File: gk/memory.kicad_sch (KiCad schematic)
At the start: 18 parts, among them J4 Micro_SD_Card_Det2, U6 IS42S16320F-7TLI-TR

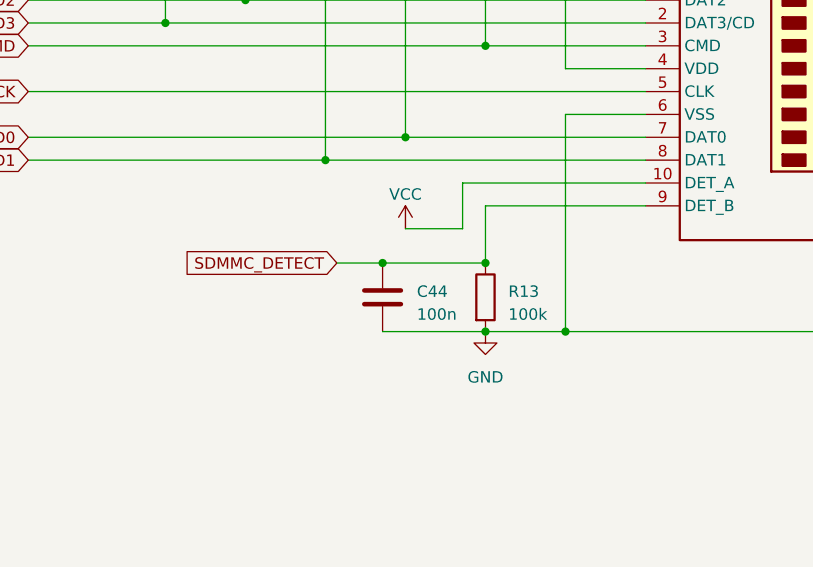
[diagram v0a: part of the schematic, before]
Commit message: remove SD detect
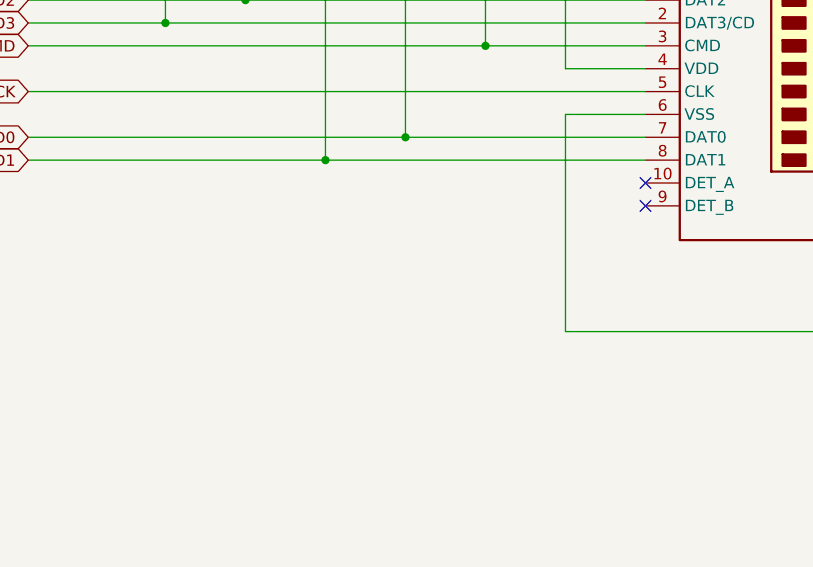
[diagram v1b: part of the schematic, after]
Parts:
- removed C44: 100n, Capacitor_SMD:C_0603_1608Metric, symbol Device:C
- removed R13: 100k, Resistor_SMD:R_0603_1608Metric, symbol Device:R
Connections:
- net GND: no longer J4.11 (SHIELD), J4.6 (VSS)
- net VCC: no longer J4.10 (DET_A)
- net SDMMC_DETECT: no longer names the net of J4.9 (DET_B)
- new net: J4.11 (SHIELD), J4.6 (VSS)
- no-connect marks 0 -> 2
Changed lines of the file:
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@@
   (junction (at 69.85 68.58) (diameter 0) (color 0 0 0 0)
   )
-  (junction (at 224.79 100.33) (diameter 0) (color 0 0 0 0)
-  )
   (junction (at 49.53 53.34) (diameter 0) (color 0 0 0 0)
   )
@@
   (junction (at 38.1 53.34) (diameter 0) (color 0 0 0 0)
   )
-  (junction (at 215.9 92.71) (diameter 0) (color 0 0 0 0)
-  )
   (junction (at 224.79 40.64) (diameter 0) (color 0 0 0 0)
   )
@@
   (junction (at 72.39 45.72) (diameter 0) (color 0 0 0 0)
   )
-  (junction (at 215.9 100.33) (diameter 0) (color 0 0 0 0)
-  )
   (junction (at 207.01 40.64) (diameter 0) (color 0 0 0 0)
   )
@@
   (junction (at 95.25 45.72) (diameter 0) (color 0 0 0 0)
   )
-  (junction (at 204.47 92.71) (diameter 0) (color 0 0 0 0)
-  )
   (junction (at 60.96 45.72) (diameter 0) (color 0 0 0 0)
   )
@@
   (junction (at 215.9 40.64) (diameter 0) (color 0 0 0 0)
   )
+  (no_connect (at 233.68 86.36))
+  (no_connect (at 233.68 83.82))
   (wire (pts (xy 71.12 74.93) (xy 71.12 68.58))
     (stroke (width 0) (type default))
@@
     (stroke (width 0) (type default))
   )
-  (wire (pts (xy 204.47 100.33) (xy 215.9 100.33))
-    (stroke (width 0) (type default))
-  )
   (wire (pts (xy 232.41 40.64) (xy 245.11 40.64))
     (stroke (width 0) (type default))
@@
     (stroke (width 0) (type default))
   )
-  (wire (pts (xy 215.9 86.36) (xy 233.68 86.36))
-    (stroke (width 0) (type default))
-  )
   (wire (pts (xy 69.85 68.58) (xy 69.85 66.04))
     (stroke (width 0) (type default))
@@
     (stroke (width 0) (type default))
   )
-  (wire (pts (xy 199.39 92.71) (xy 204.47 92.71))
-    (stroke (width 0) (type default))
-  )
   (wire (pts (xy 215.9 55.88) (xy 215.9 68.58))
     (stroke (width 0) (type default))
@@
     (stroke (width 0) (type default))
   )
-  (wire (pts (xy 233.68 83.82) (xy 213.36 83.82))
-    (stroke (width 0) (type default))
-  )
   (wire (pts (xy 49.53 53.34) (xy 60.96 53.34))
     (stroke (width 0) (type default))
@@
     (stroke (width 0) (type default))
   )
-  (wire (pts (xy 204.47 92.71) (xy 215.9 92.71))
-    (stroke (width 0) (type default))
-  )
   (wire (pts (xy 189.23 48.26) (xy 189.23 40.64))
     (stroke (width 0) (type default))
@@
     (stroke (width 0) (type default))
   )
-  (wire (pts (xy 215.9 92.71) (xy 215.9 86.36))
-    (stroke (width 0) (type default))
-  )
   (wire (pts (xy 198.12 55.88) (xy 198.12 81.28))
     (stroke (width 0) (type default))
@@
     (stroke (width 0) (type default))
   )
-  (wire (pts (xy 213.36 83.82) (xy 213.36 88.9))
-    (stroke (width 0) (type default))
-  )
   (wire (pts (xy 198.12 40.64) (xy 207.01 40.64))
     (stroke (width 0) (type default))
@@
     (stroke (width 0) (type default))
   )
-  (wire (pts (xy 213.36 88.9) (xy 207.01 88.9))
-    (stroke (width 0) (type default))
-  )
   (wire (pts (xy 215.9 48.26) (xy 215.9 40.64))
-    (stroke (width 0) (type default))
-  )
-  (wire (pts (xy 224.79 100.33) (xy 215.9 100.33))
     (stroke (width 0) (type default))
   )
@@
     )
   )
-  (global_label "SDMMC_DETECT" (shape input) (at 199.39 92.71 180) (fields_autoplaced)
-    (effects (font (size 1.27 1.27)) (justify right))
-    (property "Intersheetrefs" "${INTERSHEET_REFS}" (at 182.0911 92.71 0)
-      (effects (font (size 1.27 1.27)) (justify right) hide)
-    )
-  )
   (global_label "FMC_SDNCAS" (shape input) (at 58.42 138.43 180) (fields_autoplaced)
     (effects (font (size 1.27 1.27)) (justify right))
@@
         (path "/08730ac6-6084-459f-bdf1-86b322355ede/ac7bc38d-62b1-41db-b7cb-3988a99ad24d"
           (reference "C46") (unit 1)
-        )
-      )
-    )
-  )
-  (symbol (lib_id "power:GND") (at 215.9 100.33 0) (unit 1)
-    (in_bom yes) (on_board yes) (dnp no) (fields_autoplaced)
-    (property "Reference" "#PWR021" (at 215.9 106.68 0)
-      (effects (font (size 1.27 1.27)) hide)
-    )
-    (property "Value" "GND" (at 215.9 105.41 0)
-      (effects (font (size 1.27 1.27)))
-    )
-    (property "Footprint" "" (at 215.9 100.33 0)
-      (effects (font (size 1.27 1.27)) hide)
-    )
-    (property "Datasheet" "" (at 215.9 100.33 0)
-      (effects (font (size 1.27 1.27)) hide)
-    )
-    (pin "1")
-    (instances
-      (project "gk"
-        (path "/08730ac6-6084-459f-bdf1-86b322355ede/ac7bc38d-62b1-41db-b7cb-3988a99ad24d"
-          (reference "#PWR021") (unit 1)
         )
       )
@@
     )
   )
-  (symbol (lib_id "Device:C") (at 204.47 96.52 0) (unit 1)
-    (in_bom yes) (on_board yes) (dnp no) (fields_autoplaced)
-    (property "Reference" "C44" (at 208.28 95.885 0)
-      (effects (font (size 1.27 1.27)) (justify left))
-    )
-    (property "Value" "100n" (at 208.28 98.425 0)
-      (effects (font (size 1.27 1.27)) (justify left))
-    )
-    (property "Footprint" "Capacitor_SMD:C_0603_1608Metric" (at 205.4352 100.33 0)
-      (effects (font (size 1.27 1.27)) hide)
-    )
-    (property "Datasheet" "~" (at 204.47 96.52 0)
-      (effects (font (size 1.27 1.27)) hide)
-    )
-    (pin "1")
-    (pin "2")
-    (instances
-      (project "gk"
-        (path "/08730ac6-6084-459f-bdf1-86b322355ede/ac7bc38d-62b1-41db-b7cb-3988a99ad24d"
-          (reference "C44") (unit 1)
-        )
-      )
-    )
-  )
-  (symbol (lib_id "Device:R") (at 215.9 96.52 0) (unit 1)
-    (in_bom yes) (on_board yes) (dnp no) (fields_autoplaced)
-    (property "Reference" "R13" (at 218.44 95.885 0)
-      (effects (font (size 1.27 1.27)) (justify left))
-    )
-    (property "Value" "100k" (at 218.44 98.425 0)
-      (effects (font (size 1.27 1.27)) (justify left))
-    )
-    (property "Footprint" "Resistor_SMD:R_0603_1608Metric" (at 214.122 96.52 90)
-      (effects (font (size 1.27 1.27)) hide)
-    )
-    (property "Datasheet" "~" (at 215.9 96.52 0)
-      (effects (font (size 1.27 1.27)) hide)
-    )
-    (pin "1")
-    (pin "2")
-    (instances
-      (project "gk"
-        (path "/08730ac6-6084-459f-bdf1-86b322355ede/ac7bc38d-62b1-41db-b7cb-3988a99ad24d"
-          (reference "R13") (unit 1)
-        )
-      )
-    )
-  )
   (symbol (lib_id "Device:C") (at 95.25 49.53 0) (unit 1)
     (in_bom yes) (on_board yes) (dnp no) (fields_autoplaced)
@@
         )
       )
-    )
-  )
-  (symbol (lib_id "power:VCC") (at 207.01 88.9 0) (unit 1)
-    (in_bom yes) (on_board yes) (dnp no) (fields_autoplaced)
-    (property "Reference" "#PWR020" (at 207.01 92.71 0)
-      (effects (font (size 1.27 1.27)) hide)
-    )
-    (property "Value" "VCC" (at 207.01 85.09 0)
-      (effects (font (size 1.27 1.27)))
-    )
-    (property "Footprint" "" (at 207.01 88.9 0)
-      (effects (font (size 1.27 1.27)) hide)
-    )
-    (property "Datasheet" "" (at 207.01 88.9 0)
-      (effects (font (size 1.27 1.27)) hide)
-    )
-    (pin "1")
-    (instances
-      (project "gk"
-        (path "/08730ac6-6084-459f-bdf1-86b322355ede/ac7bc38d-62b1-41db-b7cb-3988a99ad24d"
-          (reference "#PWR020") (unit 1)
-        )
-      )

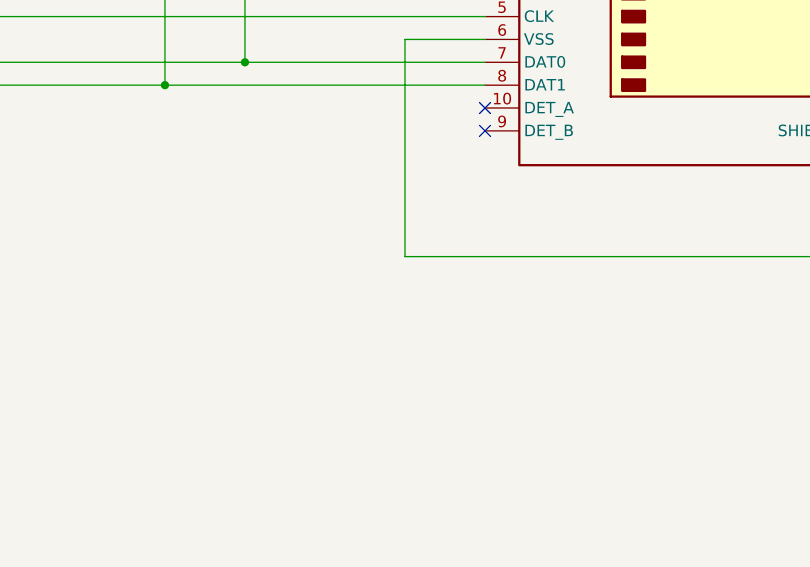
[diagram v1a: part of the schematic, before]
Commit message: Add winc uart programming header
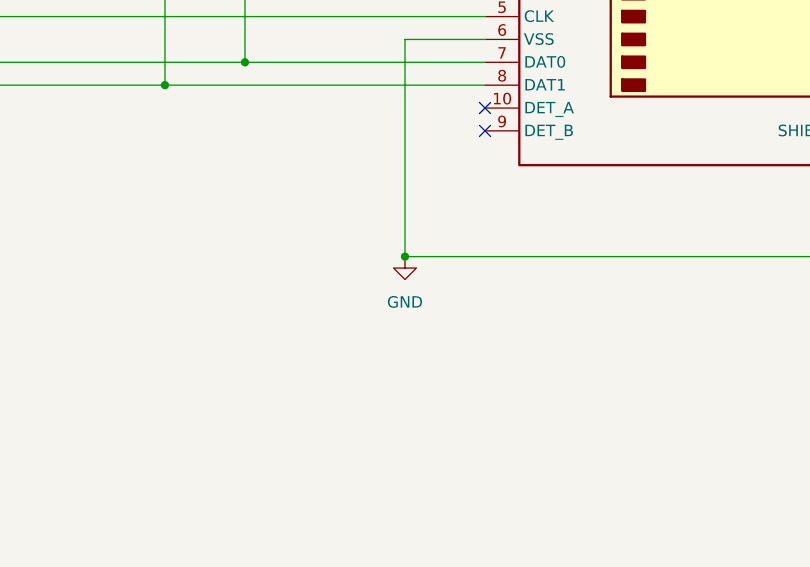
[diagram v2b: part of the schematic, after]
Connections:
- net GND: now also J4.11 (SHIELD), J4.6 (VSS)
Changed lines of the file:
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@@
   (junction (at 49.53 53.34) (diameter 0) (color 0 0 0 0)
+  )
+  (junction (at 224.79 100.33) (diameter 0) (color 0 0 0 0)
   )
   (junction (at 198.12 81.28) (diameter 0) (color 0 0 0 0)
@@
         )
       )
+    )
+  )
+  (symbol (lib_id "power:GND") (at 224.79 100.33 0) (unit 1)
+    (in_bom yes) (on_board yes) (dnp no) (fields_autoplaced)
+    (property "Reference" "#PWR020" (at 224.79 106.68 0)
+      (effects (font (size 1.27 1.27)) hide)
+    )
+    (property "Value" "GND" (at 224.79 105.41 0)
+      (effects (font (size 1.27 1.27)))
+    )
+    (property "Footprint" "" (at 224.79 100.33 0)
+      (effects (font (size 1.27 1.27)) hide)
+    )
+    (property "Datasheet" "" (at 224.79 100.33 0)
+      (effects (font (size 1.27 1.27)) hide)
+    )
+    (pin "1")
+    (instances
+      (project "gk"
+        (path "/08730ac6-6084-459f-bdf1-86b322355ede/ac7bc38d-62b1-41db-b7cb-3988a99ad24d"
+          (reference "#PWR020") (unit 1)
+        )
+      )

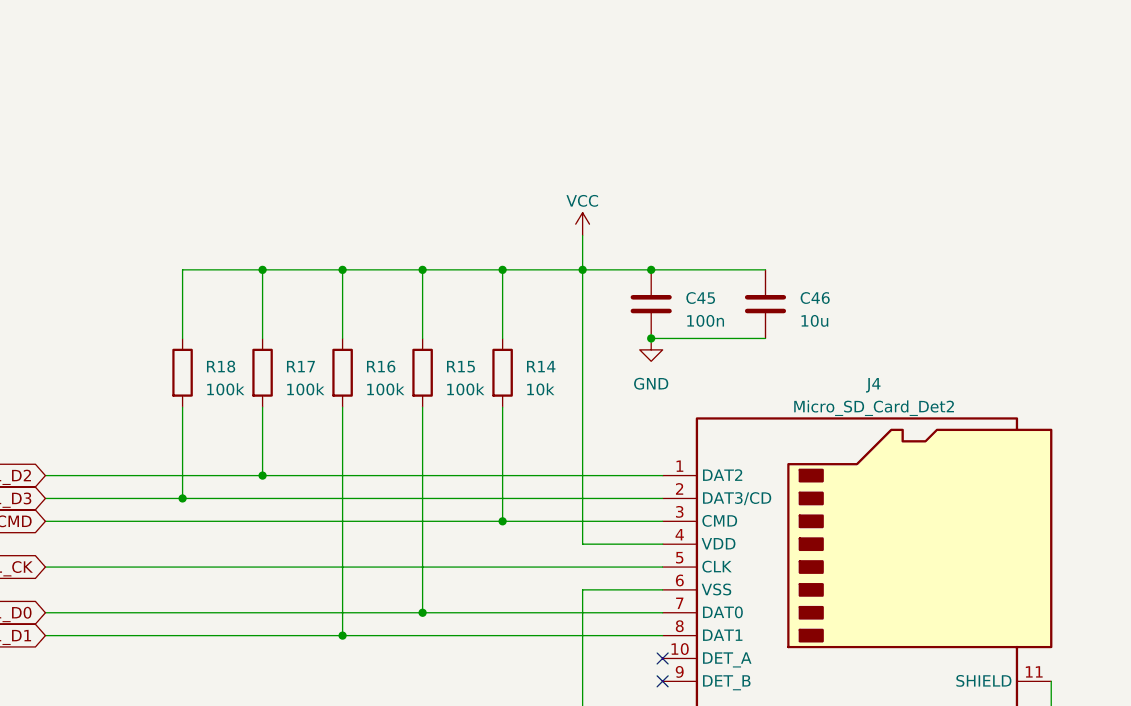
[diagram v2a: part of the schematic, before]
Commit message: Add SD power switch
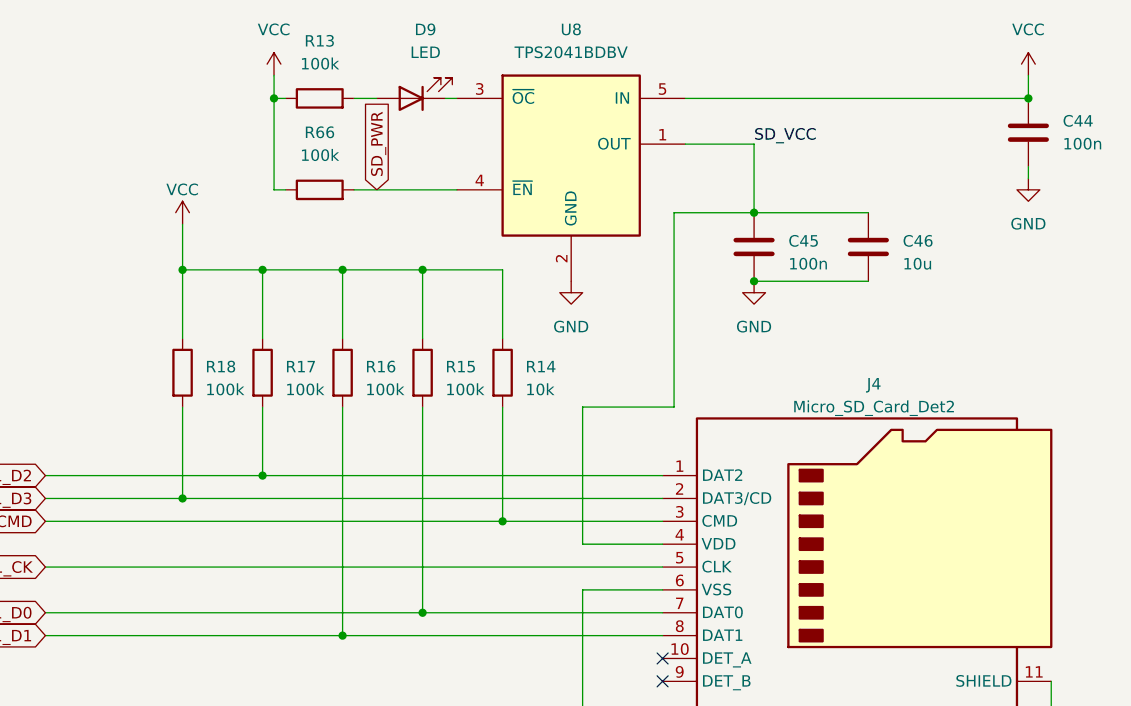
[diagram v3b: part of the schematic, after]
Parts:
- added C44: 100n, Capacitor_SMD:C_0603_1608Metric, symbol Device:C
- added D9: LED, LED_SMD:LED_0603_1608Metric, symbol Device:LED
- added R13, R66: 100k, Resistor_SMD:R_0603_1608Metric, symbol Device:R
- added U8: TPS2041BDBV, Package_TO_SOT_SMD:SOT-23-5, symbol Power_Management:TPS2041B
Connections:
- net GND: now also C44.2, U8.2 (GND)
- net VCC: now also C44.1, R13.1, R66.1, U8.5 (IN); no longer C45.1, C46.1, J4.4 (VDD)
- new net: D9.1 (K), U8.3 (~{OC})
- new net: D9.2 (A), R13.2
- new net SD_PWR: R66.2, U8.4 (~{EN})
- new net SD_VCC: C45.1, C46.1, J4.4 (VDD), U8.1 (OUT)
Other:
- moved on the sheet: C45, C46
